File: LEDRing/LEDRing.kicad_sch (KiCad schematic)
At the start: 5 parts, among them J1 V+, J2 V-

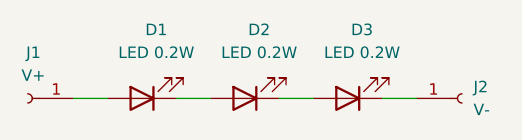
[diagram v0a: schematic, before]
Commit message: Ring hole size increased
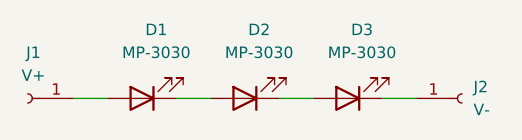
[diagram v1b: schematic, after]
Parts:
- D1, D2, D3: value LED 0.2W -> MP-3030
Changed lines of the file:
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@@
 			)
 		)
-		(property "Value" "LED 0.2W"
+		(property "Value" "MP-3030"
 			(at 119.6975 57.15 0)
 			(effects
@@
 			)
 		)
-		(property "Value" "LED 0.2W"
+		(property "Value" "MP-3030"
 			(at 108.2675 57.15 0)
 			(effects
@@
 			)
 		)
-		(property "Value" "LED 0.2W"
+		(property "Value" "MP-3030"
 			(at 96.8375 57.15 0)
 			(effects
